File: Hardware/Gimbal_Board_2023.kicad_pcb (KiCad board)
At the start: 2 copper layers, 72 parts, among them J1 6P6C, J2 RJ45_LED_Shielded, Q1 Q_NMOS_GDS, Q2 Q_NMOS_GDS, Q3 Q_NMOS_GDS, Q4 Q_NMOS_GDS, Q5 Q_NMOS_GDS, Q6 Q_NMOS_GDS, Q7 Q_NMOS_GDS, SW1 SW_Push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

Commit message: Connected leds for servos
Connected leds for servos
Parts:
- moved R25 0.27 mm to (194.6, 69.0)
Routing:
- net Net-(DB7-Pad1): track 0.00 -> 2.61 mm
- net Net-(Q5-Pad1): track 0.00 -> 2.24 mm
- net Net-(Q7-Pad1): track 0.00 -> 2.23 mm
- net Net-(Q4-Pad1): track 0.00 -> 2.20 mm
- net Net-(DB6-Pad1): track 0.00 -> 2.19 mm
- net Net-(DB4-Pad1): track 0.00 -> 2.14 mm
- net Net-(Q3-Pad1): track 0.00 -> 2.12 mm
- net Net-(Q2-Pad1): track 0.00 -> 2.06 mm
- net Net-(DB7-Pad2): track 0.00 -> 2.04 mm
- net Net-(DB5-Pad1): track 0.00 -> 2.03 mm
- net Net-(DB6-Pad2): track 0.00 -> 1.96 mm
- net Net-(Q6-Pad1): track 0.00 -> 1.94 mm
- net Net-(DB3-Pad1): track 0.00 -> 1.86 mm
- net Net-(DB4-Pad2): track 0.00 -> 1.83 mm
- net Net-(DB3-Pad2): track 0.00 -> 1.83 mm
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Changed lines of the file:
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@@
   )
   (footprint "Resistor_SMD:R_0603_1608Metric_Pad0.98x0.95mm_HandSolder" (layer "F.Cu")
-    (at 194.296 68.9845 90)
+    (at 194.564 68.9845 90)
     (descr "Resistor SMD 0603 (1608 Metric), square (rectangular) end terminal, IPC_7351 nominal with elongated pad for handsoldering. (Body size source: IPC-SM-782 page 72, https://www.pcb-3d.com/wordpress/wp-content/uploads/ipc-sm-782a_amendment_1_and_2.pdf), generated with kicad-footprint-generator")
     (tags "resistor handsolder")
@@
   (segment (start 118.336 66.294) (end 118.336 68.044) (width 0.25) (layer "F.Cu") (net 5))
   (segment (start 118.336 68.044) (end 118.364 68.072) (width 0.25) (layer "F.Cu") (net 5))
+  (segment (start 128.905 66.294) (end 130.711 66.294) (width 0.25) (layer "F.Cu") (net 6))
+  (segment (start 132.461 66.294) (end 132.461 68.072) (width 0.25) (layer "F.Cu") (net 7))
+  (segment (start 141.845 66.04) (end 143.524 66.04) (width 0.25) (layer "F.Cu") (net 8))
+  (segment (start 143.524 66.04) (end 143.651 66.167) (width 0.25) (layer "F.Cu") (net 8))
+  (segment (start 145.401 66.167) (end 145.401 67.818) (width 0.25) (layer "F.Cu") (net 9))
+  (segment (start 145.401 67.818) (end 145.528 67.945) (width 0.25) (layer "F.Cu") (net 9))
+  (segment (start 153.35 66.001) (end 155.437 66.001) (width 0.25) (layer "F.Cu") (net 10))
+  (segment (start 155.437 66.001) (end 155.476 66.04) (width 0.25) (layer "F.Cu") (net 10))
+  (segment (start 157.226 66.04) (end 157.226 67.691) (width 0.25) (layer "F.Cu") (net 11))
+  (segment (start 157.226 67.691) (end 157.353 67.818) (width 0.25) (layer "F.Cu") (net 11))
+  (segment (start 165.782 66.2155) (end 167.7025 66.2155) (width 0.25) (layer "F.Cu") (net 12))
+  (segment (start 167.7025 66.2155) (end 167.781 66.294) (width 0.25) (layer "F.Cu") (net 12))
+  (segment (start 169.531 66.294) (end 169.531 68.072) (width 0.25) (layer "F.Cu") (net 13))
+  (segment (start 178.355 66.264) (end 180.324 66.264) (width 0.25) (layer "F.Cu") (net 14))
+  (segment (start 180.324 66.264) (end 180.481 66.421) (width 0.25) (layer "F.Cu") (net 14))
+  (segment (start 182.231 66.421) (end 182.231 68.199) (width 0.25) (layer "F.Cu") (net 15))
+  (segment (start 182.231 68.199) (end 182.358 68.326) (width 0.25) (layer "F.Cu") (net 15))
+  (segment (start 190.227 65.913) (end 192.659 65.913) (width 0.25) (layer "F.Cu") (net 16))
+  (segment (start 192.659 65.913) (end 192.786 66.04) (width 0.25) (layer "F.Cu") (net 16))
+  (segment (start 194.564 66.068) (end 194.536 66.04) (width 0.25) (layer "F.Cu") (net 17))
+  (segment (start 194.564 68.072) (end 194.564 66.068) (width 0.25) (layer "F.Cu") (net 17))
   (segment (start 89.525 58.9875) (end 89.525 52.95) (width 0.25) (layer "F.Cu") (net 18))
   (segment (start 117.561 109.855) (end 121.752 109.855) (width 0.25) (layer "F.Cu") (net 19))
@@
   (segment (start 112.856 68.326) (end 112.856 66.369) (width 0.25) (layer "F.Cu") (net 36))
   (segment (start 112.856 66.369) (end 112.781 66.294) (width 0.25) (layer "F.Cu") (net 36))
+  (segment (start 127.08 68.326) (end 127.08 66.369) (width 0.25) (layer "F.Cu") (net 37))
+  (segment (start 127.08 66.369) (end 127.005 66.294) (width 0.25) (layer "F.Cu") (net 37))
+  (segment (start 139.945 66.04) (end 139.945 67.87) (width 0.25) (layer "F.Cu") (net 38))
+  (segment (start 139.945 67.87) (end 140.147 68.072) (width 0.25) (layer "F.Cu") (net 38))
+  (segment (start 151.45 66.001) (end 151.45 68.185) (width 0.25) (layer "F.Cu") (net 39))
+  (segment (start 151.45 68.185) (end 151.464 68.199) (width 0.25) (layer "F.Cu") (net 39))
+  (segment (start 163.882 68.439) (end 163.896 68.453) (width 0.25) (layer "F.Cu") (net 40))
+  (segment (start 163.882 66.2155) (end 163.882 68.439) (width 0.25) (layer "F.Cu") (net 40))
+  (segment (start 176.455 66.264) (end 176.455 68.185) (width 0.25) (layer "F.Cu") (net 41))
+  (segment (start 176.455 68.185) (end 176.469 68.199) (width 0.25) (layer "F.Cu") (net 41))
+  (segment (start 188.327 65.913) (end 188.327 67.898) (width 0.25) (layer "F.Cu") (net 42))
+  (segment (start 188.327 67.898) (end 188.153 68.072) (width 0.25) (layer "F.Cu") (net 42))
   (segment (start 121.679 102.997) (end 119.552 100.87) (width 0.25) (layer "F.Cu") (net 43))
   (segment (start 119.552 100.87) (end 125.172 95.25) (width 0.25) (layer "F.Cu") (net 43))
@@
   (segment (start 132.461 69.897) (end 134.239 68.119) (width 0.25) (layer "F.Cu") (net 59))
   (segment (start 156.21 56.769) (end 159.131 59.69) (width 0.25) (layer "F.Cu") (net 59))
-  (segment (start 194.296 69.897) (end 198.12 66.073) (width 0.25) (layer "F.Cu") (net 59))
   (segment (start 118.364 69.897) (end 120.65 67.611) (width 0.25) (layer "F.Cu") (net 59))
   (segment (start 120.65 67.611) (end 120.65 63.881) (width 0.25) (layer "F.Cu") (net 59))
@@
   (segment (start 116.84 51.943) (end 124.968 60.071) (width 0.25) (layer "F.Cu") (net 59))
   (segment (start 134.239 61.849) (end 136.017 60.071) (width 0.25) (layer "F.Cu") (net 59))
+  (segment (start 195.707 60.071) (end 193.04 60.071) (width 0.25) (layer "F.Cu") (net 59))
   (segment (start 146.812 68.486) (end 146.812 60.071) (width 0.25) (layer "F.Cu") (net 59))
   (segment (start 182.358 70.151) (end 184.15 68.359) (width 0.25) (layer "F.Cu") (net 59))
-  (segment (start 198.12 62.484) (end 195.707 60.071) (width 0.25) (layer "F.Cu") (net 59))
   (segment (start 159.131 67.865) (end 159.131 60.071) (width 0.25) (layer "F.Cu") (net 59))
   (segment (start 157.353 69.643) (end 159.131 67.865) (width 0.25) (layer "F.Cu") (net 59))
+  (segment (start 198.12 62.484) (end 195.707 60.071) (width 0.25) (layer "F.Cu") (net 59))
+  (segment (start 198.12 66.341) (end 198.12 62.484) (width 0.25) (layer "F.Cu") (net 59))
+  (segment (start 194.564 69.897) (end 198.12 66.341) (width 0.25) (layer "F.Cu") (net 59))
   (segment (start 146.812 59.944) (end 146.812 60.071) (width 0.25) (layer "F.Cu") (net 59))
   (segment (start 102.743 51.943) (end 116.84 51.943) (width 0.25) (layer "F.Cu") (net 59))
-  (segment (start 198.12 66.073) (end 198.12 62.484) (width 0.25) (layer "F.Cu") (net 59))
   (segment (start 128.397 56.769) (end 128.397 60.071) (width 0.25) (layer "F.Cu") (net 59))
   (segment (start 163.83 56.769) (end 167.132 60.071) (width 0.25) (layer "F.Cu") (net 59))
@@
   (segment (start 102.743 51.943) (end 102.743 54.944) (width 0.25) (layer "F.Cu") (net 59))
   (segment (start 145.528 69.77) (end 146.812 68.486) (width 0.25) (layer "F.Cu") (net 59))
-  (segment (start 195.707 60.071) (end 193.04 60.071) (width 0.25) (layer "F.Cu") (net 59))
   (segment (start 102.743 54.944) (end 102.616 55.071) (width 0.25) (layer "F.Cu") (net 59))
   (segment (start 124.46 60.071) (end 124.968 60.071) (width 0.25) (layer "F.Cu") (net 59))

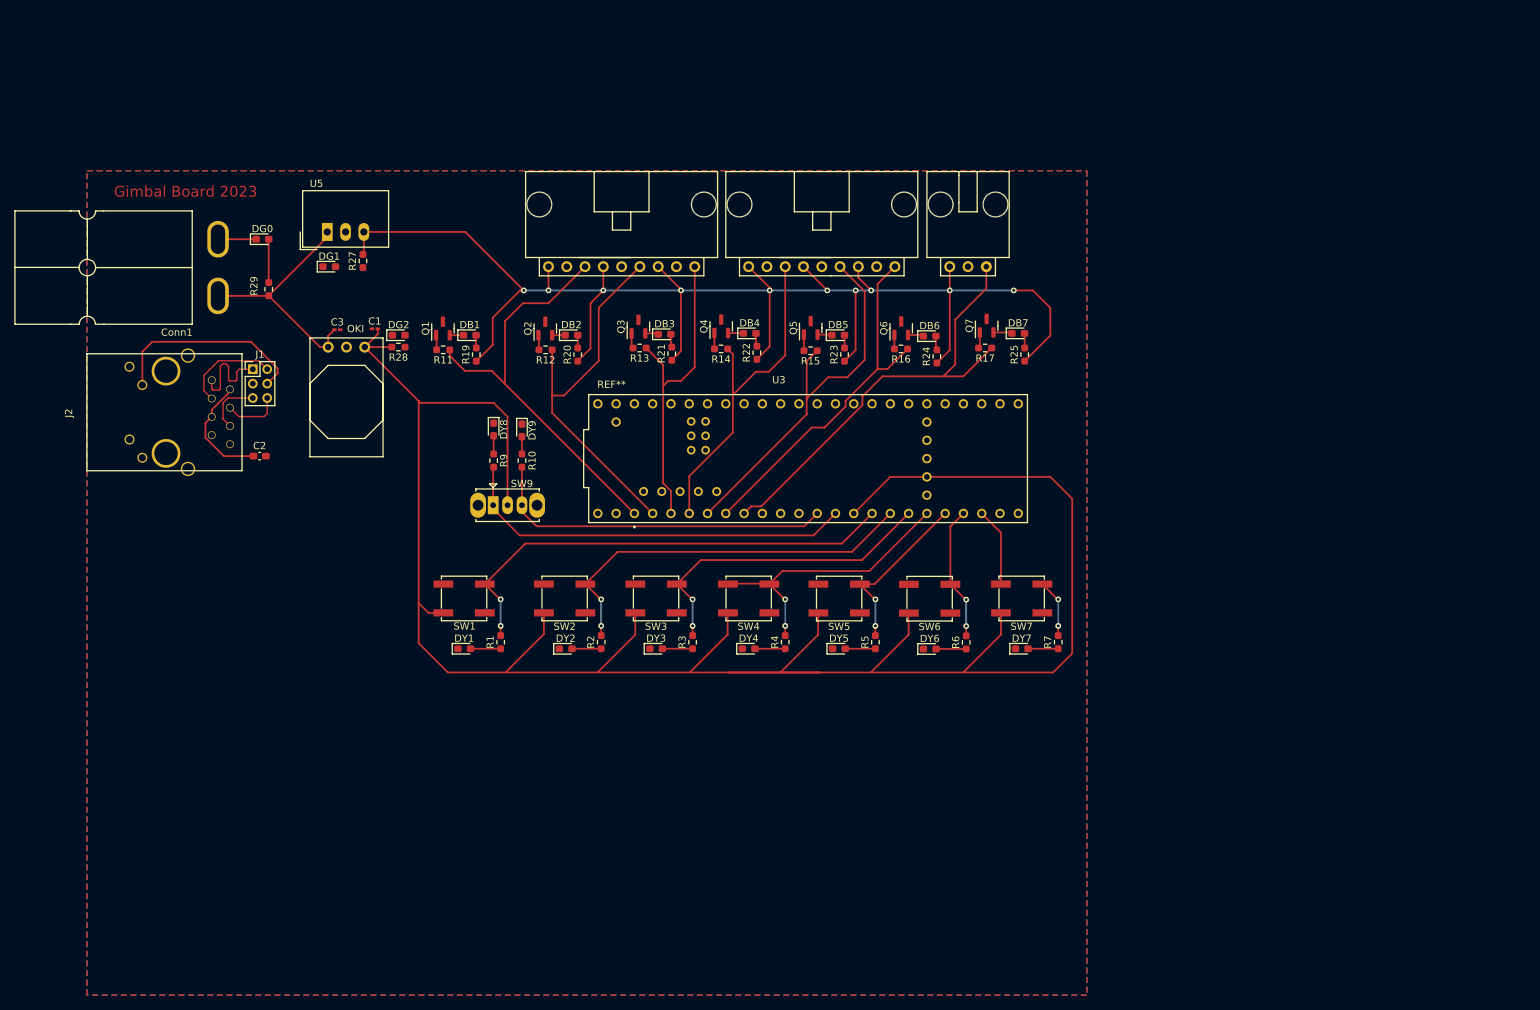
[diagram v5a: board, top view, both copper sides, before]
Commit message: Cable management, added edge cuts, and resized ground planes
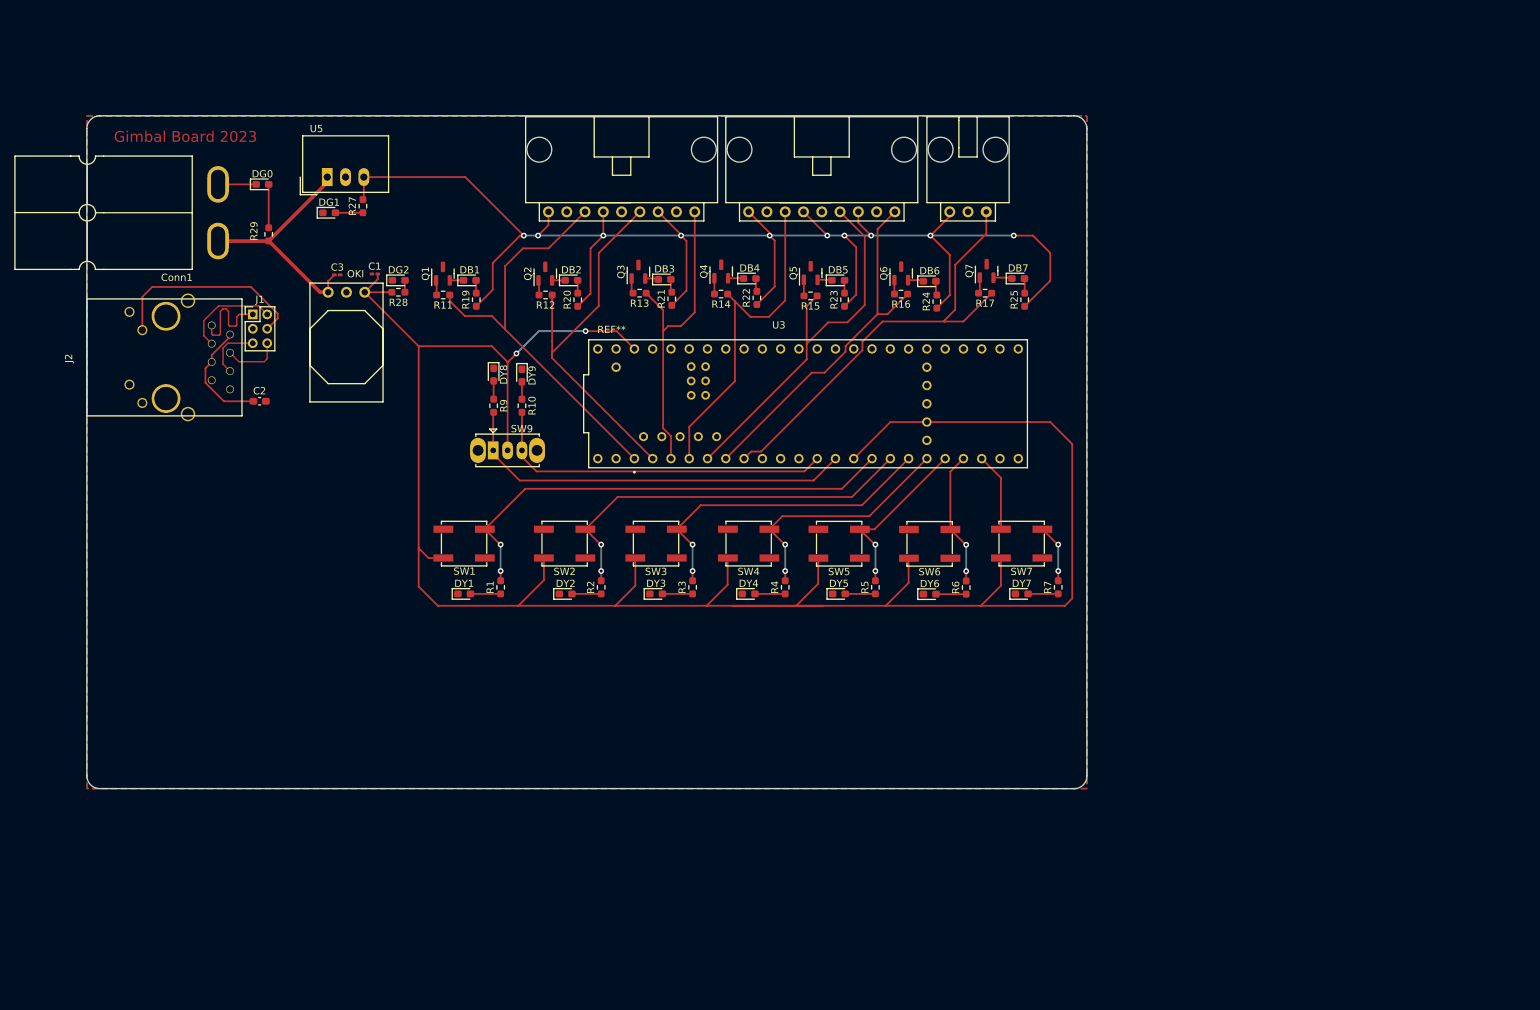
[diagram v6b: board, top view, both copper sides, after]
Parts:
- moved C1 7.62 mm to (104.3, 57.8)
- moved C2 7.62 mm to (88.3, 75.5)
- moved DB3 7.62 mm to (144.5, 58.5)
- moved DB4 7.62 mm to (156.4, 58.4)
- moved DB6 7.62 mm to (181.4, 58.8)
- moved DB7 7.62 mm to (193.7, 58.4)
- moved DG0 7.62 mm to (88.7, 45.3)
- moved DY1 7.62 mm to (116.7, 102.2)
- moved DY2 7.62 mm to (130.8, 102.2)
- moved DY3 7.62 mm to (143.4, 102.2)
- moved DY4 7.62 mm to (156.2, 102.2)
- moved DY5 7.62 mm to (168.8, 102.2)
- moved DY6 7.62 mm to (181.4, 102.3)
- moved DY7 7.62 mm to (194.2, 102.2)
- moved DY9 7.62 mm to (124.7, 71.9)
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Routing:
- net Servo_4_SW: track 39.7 -> 34.0 mm
- net +5V: track 205.5 -> 210.3 mm
- net +3.3V: track 304.2 -> 308.2 mm, vias 0 -> 2
- net Net-(DG1-Pad2): track 0.00 -> 3.82 mm
- net Net-(DG2-Pad2): track 0.00 -> 1.65 mm
- net Servo_2_PWM: track 52.4 -> 53.8 mm
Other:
- board outline added: 139 x 93.5 mm

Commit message: Rearranged components
delete trace
made board more compact
labeled
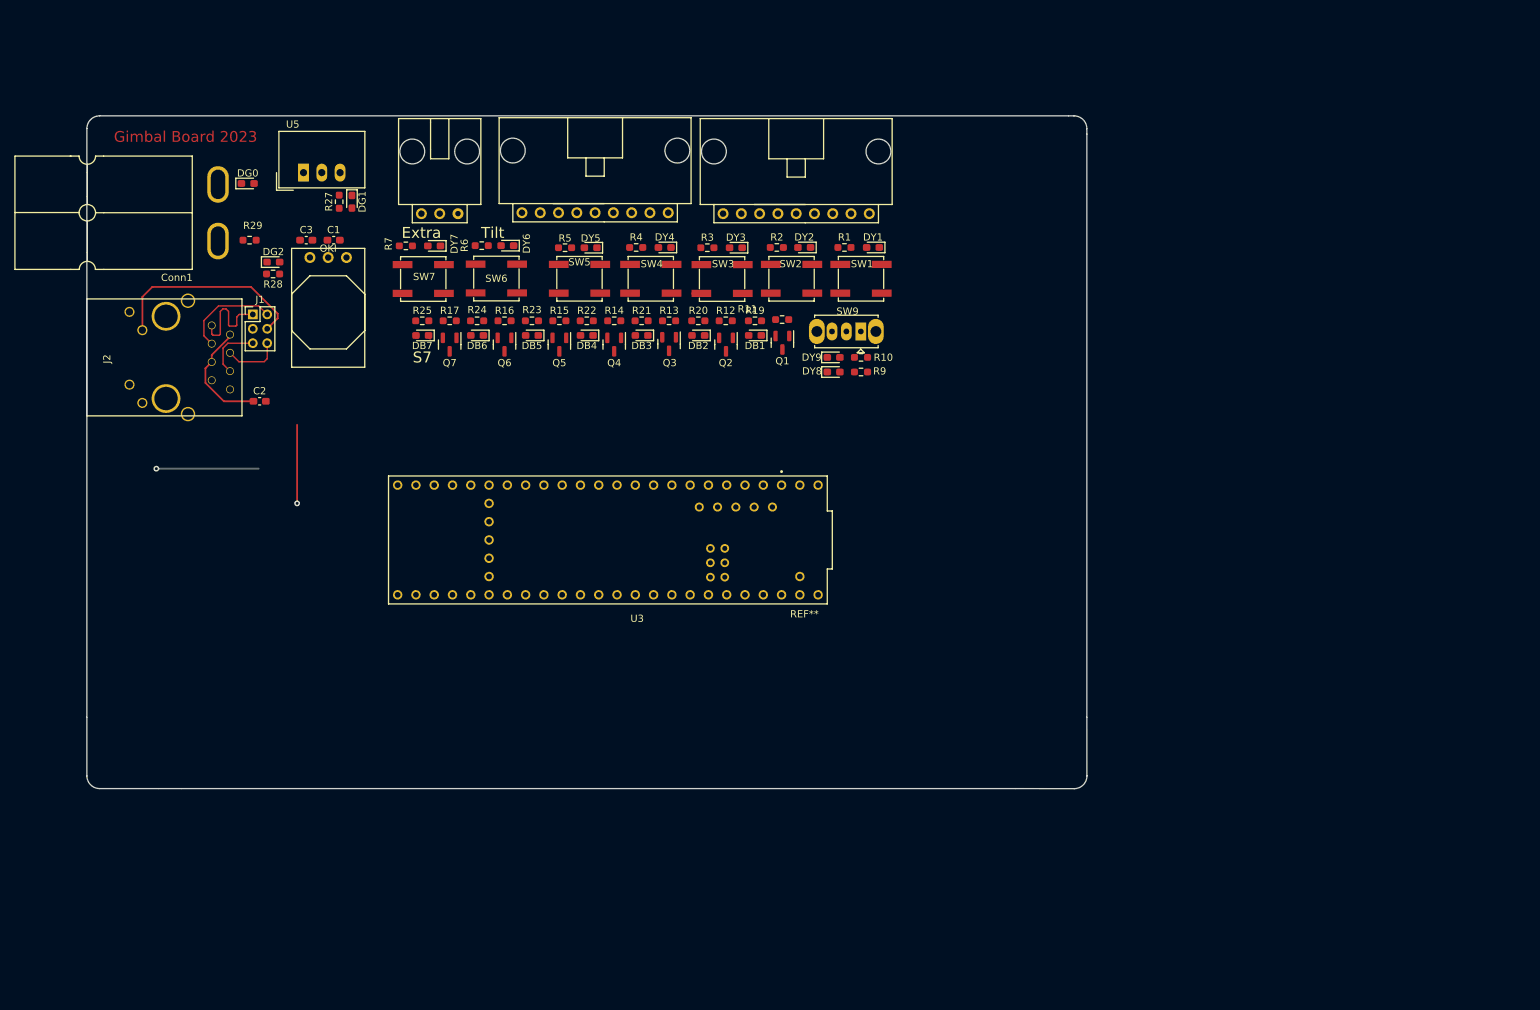
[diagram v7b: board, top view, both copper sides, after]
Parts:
- C1, C3: footprint Capacitor_SMD:C_0201_0603Metric_Pad0.64x0.40mm_HandSolder -> Capacitor_SMD:C_0603_1608Metric_Pad1.08x0.95mm_HandSolder
- moved U3 116.4 mm to (187.5, 130.3), turned to 180 degrees
- moved R7 102.3 mm to (108.6, 53.9), turned to 180 degrees
- moved DY7 94.9 mm to (112.5, 53.9), turned to 180 degrees
- moved SW7 90.9 mm to (111.0, 58.5), turned to 0 degrees
- moved R25 83.8 mm to (110.9, 64.3), turned to 0 degrees
- moved DB7 83.2 mm to (110.9, 66.3), turned to 180 degrees
- moved R6 82.4 mm to (119.1, 53.8), turned to 180 degrees
- moved DY6 76.1 mm to (122.7, 53.8), turned to 180 degrees
- moved Q7 75.3 mm to (114.7, 67.6), turned to -90 degrees
- moved R17 74.5 mm to (114.7, 64.3), turned to 0 degrees
- moved DY1 74.4 mm to (173.5, 54.1), turned to 180 degrees
- moved Conn8 73.4 mm to (110.7, 49.4)
- moved SW6 70.6 mm to (121.2, 58.4), turned to 0 degrees
- moved R1 67.2 mm to (169.5, 54.1), turned to 180 degrees
- moved SW1 66.3 mm to (171.8, 58.5), turned to 0 degrees
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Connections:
- SW1 pad 1: +3.3V -> Servo_1_SW
- SW1 pad 2: Servo_1_SW -> +3.3V
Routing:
- net +3.3V: track 308.2 -> 0.00 mm, vias 2 -> 0
- net +5V: track 210.3 -> 0.18 mm, vias 10 -> 0
- net Servo_1_SW: track 66.0 -> 0.00 mm, vias 2 -> 0
- net Servo_7_PWM: track 62.3 -> 0.00 mm
- net Servo_1_PWM: track 58.6 -> 0.00 mm
- net Servo_Manual_Control_Left: track 56.2 -> 0.00 mm
- net Servo_2_SW: track 54.5 -> 0.00 mm, vias 2 -> 0
- net Servo_2_PWM: track 53.8 -> 0.00 mm
- net Servo_5_PWM: track 53.6 -> 0.00 mm
- net Servo_6_PWM: track 50.4 -> 0.00 mm
- net Servo_Manual_Control_Right: track 48.8 -> 0.00 mm
- net Servo_4_PWM: track 47.1 -> 0.00 mm
- net Servo_3_SW: track 45.8 -> 1.46 mm, vias 2 -> 0
- net Servo_3_PWM: track 43.9 -> 0.00 mm
- net Servo_4_SW: track 34.0 -> 0.00 mm, vias 2 -> 0
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- removed copper zone on B.Cu, net GND
- removed copper zone on F.Cu, net GND
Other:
- board text added: "Extra"
- board text added: "S7"
- board text added: "Tilt"
